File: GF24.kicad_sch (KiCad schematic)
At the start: 1 part, among them U1 STM32F031C4Tx

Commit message: updated power
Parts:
- added C1, C2: 4.7uF, symbol Device:C
- added C3: 10nF, symbol Device:C
- U1: value STM32F031C4Tx -> STM32F031C4T6
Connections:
- net +3V3: now reaches U1.1 (VBAT)
- net +3V3: now also U1.24 (VDD), U1.48 (VDD), U1.9 (VDDA), C1.1, C2.1, C3.1
- net GND: now reaches U1.23 (VSS), U1.47 (VSS)
- net GND: now also U1.8 (VSSA), C1.2, C2.2, C3.2

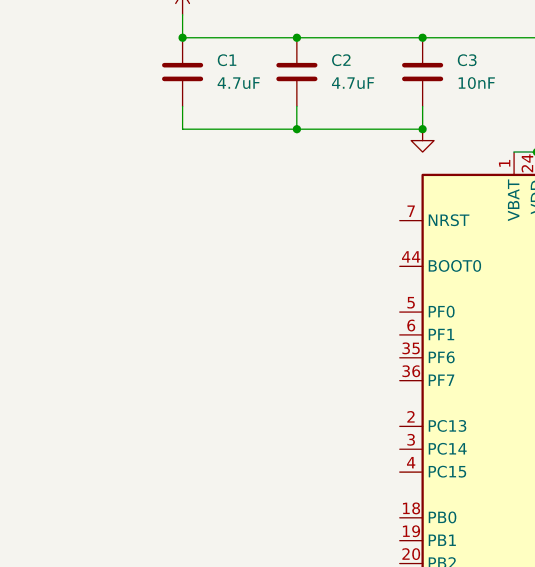
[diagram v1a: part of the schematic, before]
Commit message: changed NRST
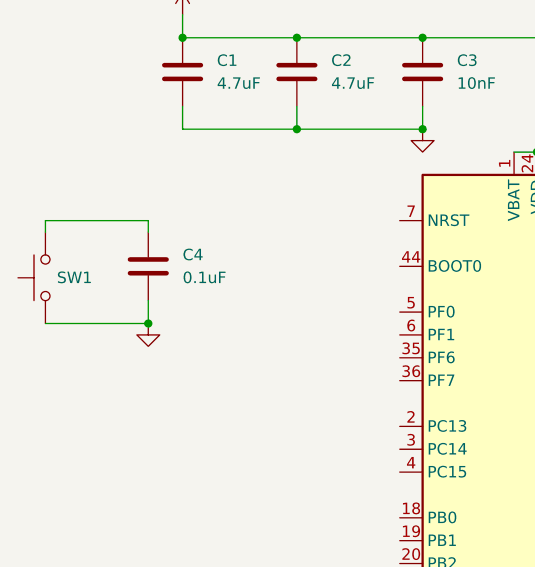
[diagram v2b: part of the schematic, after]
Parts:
- added C4: 0.1uF, symbol Device:C
- added SW1: RST, symbol Switch:SW_Push
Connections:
- net GND: now also C4.2, SW1.1
- new net: C4.1, SW1.2

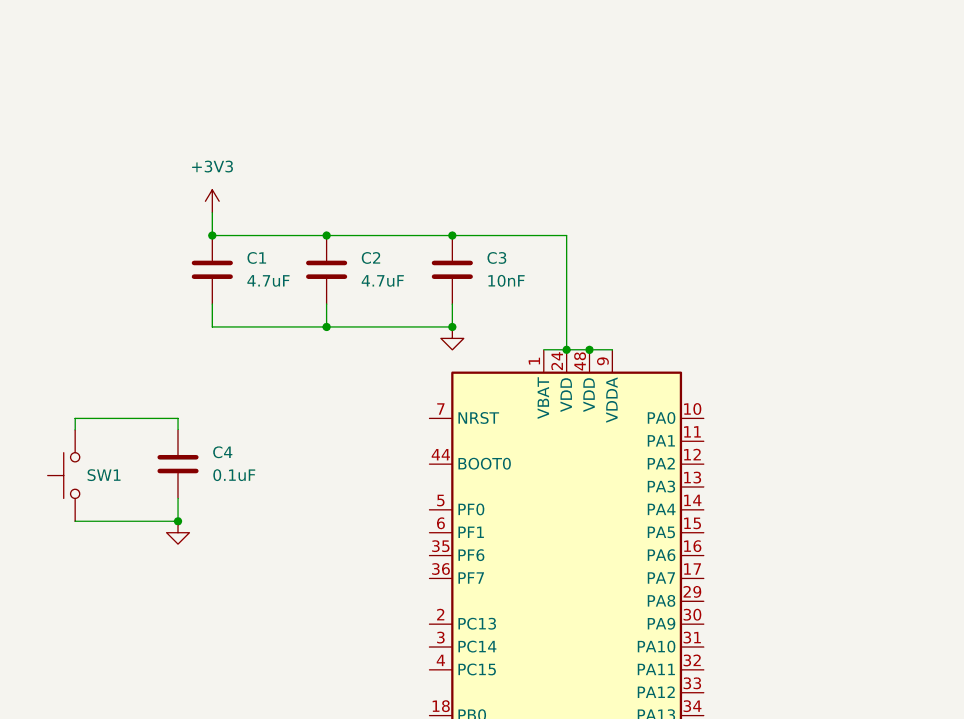
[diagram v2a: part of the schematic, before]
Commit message: sorted BOOT0 for now, added HSE
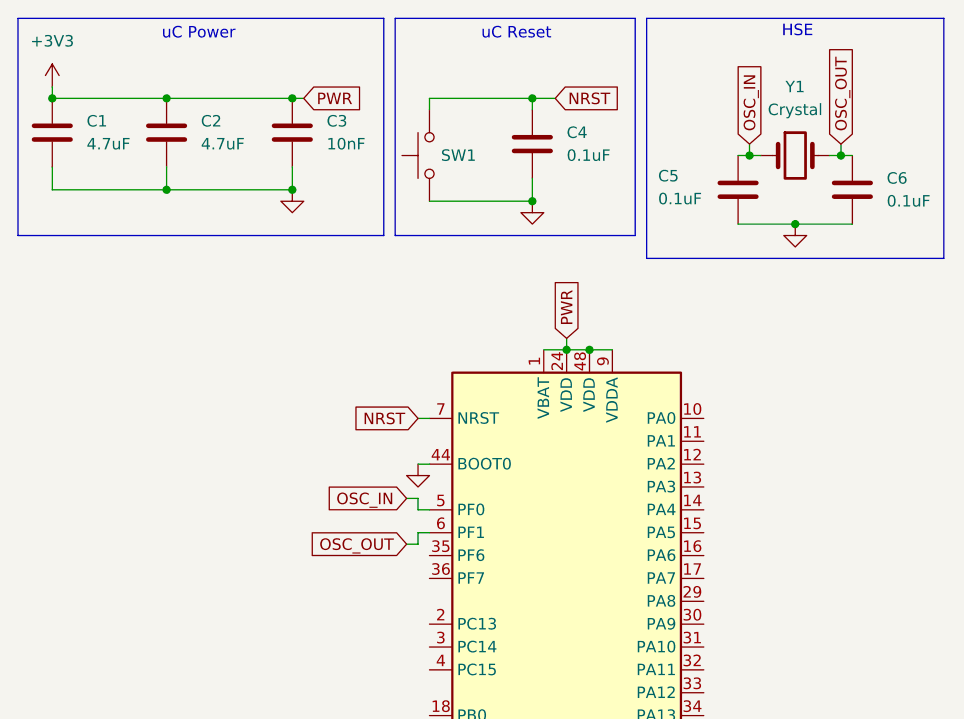
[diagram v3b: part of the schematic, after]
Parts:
- added C5, C6: 0.1uF, symbol Device:C
- added Y1: Crystal, symbol Device:Crystal
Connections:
- net GND: now also U1.44 (BOOT0), C5.2, C6.2
- net NRST: now reaches C4.1, SW1.2
- net NRST: now also U1.7 (NRST)
- net OSC_IN: now reaches U1.5 (PF0)
- net OSC_IN: now also C5.1, Y1.1
- net OSC_OUT: now reaches U1.6 (PF1)
- net OSC_OUT: now also C6.1, Y1.2
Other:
- note added: "HSE"
- note added: "uC Power"
- note added: "uC Reset"
- moved on the sheet: C1, C2, C3, C4, SW1

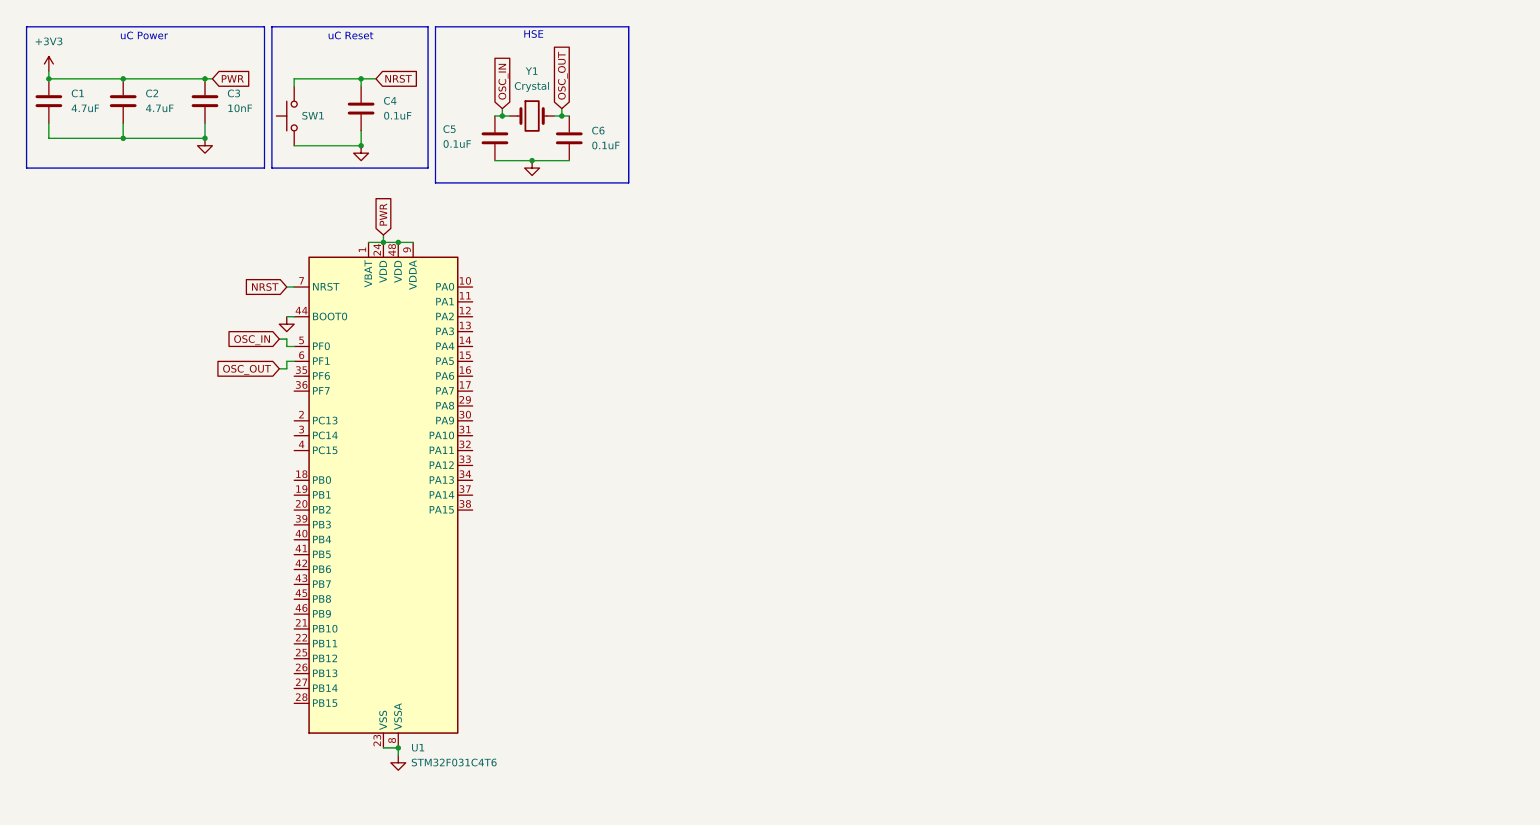
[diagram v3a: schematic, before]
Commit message: added MAX-M10S symbol/footprint
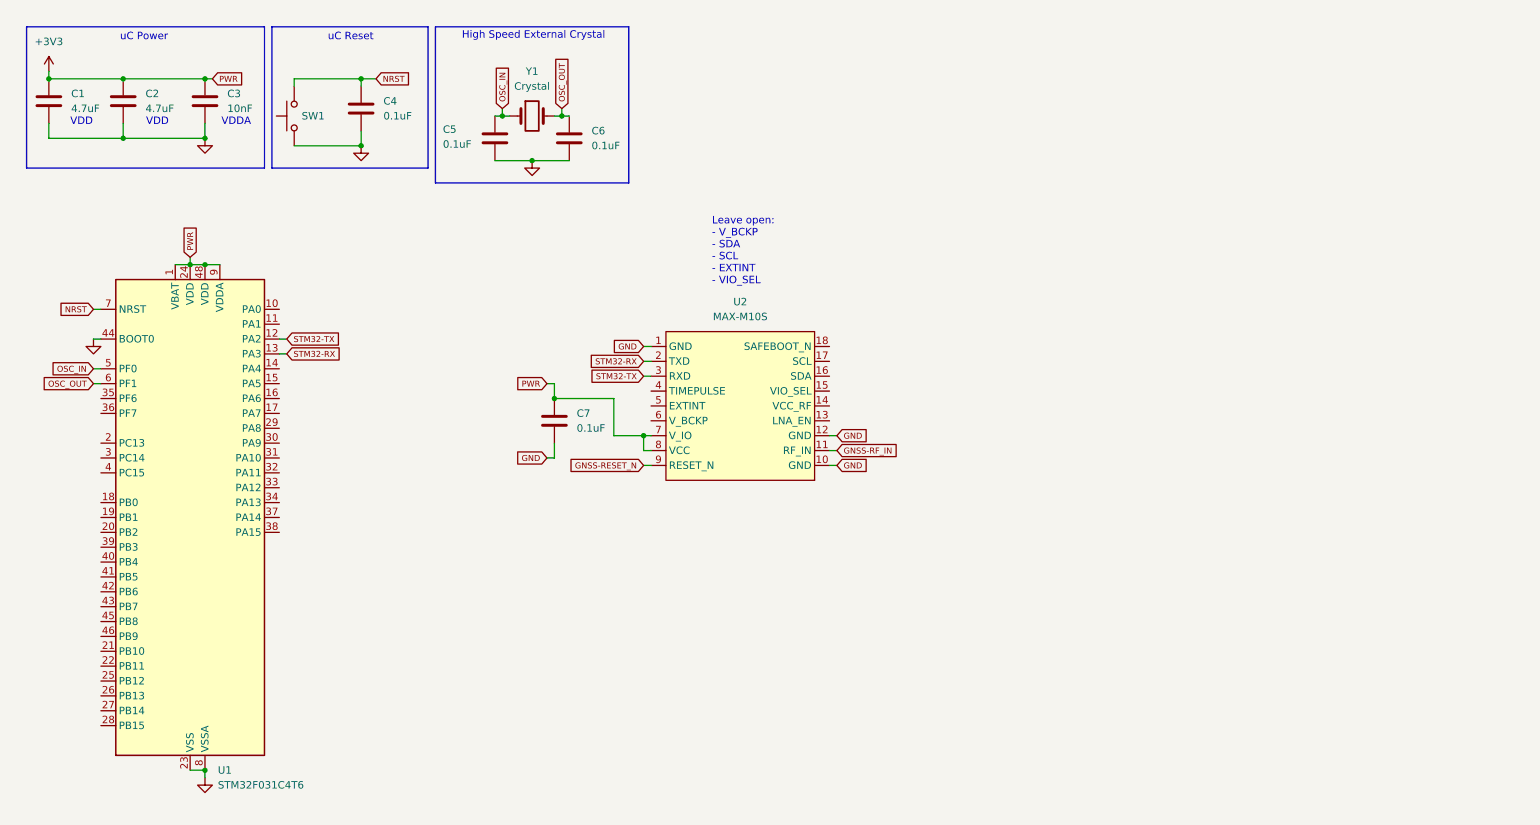
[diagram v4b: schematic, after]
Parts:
- added C7: 0.1uF, symbol Device:C
- added U2: MAX-M10S, MB-GNSS:MAX-M10S, symbol MB-GNSS:MAX-M10S
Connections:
- net +3V3: now also C7.1, U2.7 (V_IO), U2.8 (VCC)
- net GND: now also C7.2, U2.1 (GND), U2.10 (GND), U2.12 (GND)
- net STM32-TX: now reaches U1.12 (PA2)
- net STM32-TX: now also U2.3 (RXD)
- net STM32-RX: now reaches U1.13 (PA3)
- net STM32-RX: now also U2.2 (TXD)
- new net GNSS-RESET_N: U2.9 (RESET_N)
- new net GNSS-RF_IN: U2.11 (RF_IN)
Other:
- note added: "High Speed External Crystal"
- note added: "Leave open: - V_BCKP - SDA - SCL - EXTINT - VIO_SEL"
- note added: "VDD"
- note added: "VDDA"
- note removed: "HSE"
- moved on the sheet: U1

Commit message: didn't update
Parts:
- C7: value 0.1uF -> 4.7uF
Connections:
- net GNSS-RESET_N renamed GNSS-RESET-N
- net GNSS-RF_IN renamed GNSS-RF-IN
- net OSC_IN renamed OSC-IN
- net OSC_OUT renamed OSC-OUT
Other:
- note added: "Leave open: - V_BCKP - SDA - SCL - EXTINT - VIO_SEL - TIMEPULSE"
- note removed: "Leave open: - V_BCKP - SDA - SCL - EXTINT - VIO_SEL"
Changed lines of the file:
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@@
 		)
 	)
-	(text "Leave open:\n- V_BCKP\n- SDA\n- SCL\n- EXTINT\n- VIO_SEL\n"
-		(exclude_from_sim no)
-		(at 132.334 53.594 0)
+	(text "Leave open:\n- V_BCKP\n- SDA\n- SCL\n- EXTINT\n- VIO_SEL\n- TIMEPULSE"
+		(exclude_from_sim no)
+		(at 131.826 101.346 0)
 		(effects
 			(font
@@
 		)
 	)
+	(global_label "GND"
+		(shape input)
+		(at 45.72 143.51 270)
+		(fields_autoplaced yes)
+		(effects
+			(font
+				(size 1.016 1.016)
+			)
+			(justify right)
+		)
+		(property "Intersheetrefs" "${INTERSHEET_REFS}"
+			(at 45.72 148.9943 90)
+			(effects
+				(font
+					(size 1.27 1.27)
+				)
+				(justify right)
+				(hide yes)
+			)
+		)
+	)
 	(global_label "PWR"
 		(shape input)
@@
 		)
 	)
-	(global_label "GNSS-RESET_N"
+	(global_label "GNSS-RESET-N"
 		(shape input)
 		(at 120.65 90.17 180)
@@
 		)
 		(property "Intersheetrefs" "${INTERSHEET_REFS}"
-			(at 106.554 90.17 0)
+			(at 106.0702 90.17 0)
 			(effects
 				(font
@@
 		)
 	)
-	(global_label "GNSS-RF_IN"
+	(global_label "GNSS-RF-IN"
 		(shape input)
 		(at 153.67 87.63 0)
@@
 		)
 		(property "Intersheetrefs" "${INTERSHEET_REFS}"
-			(at 165.5406 87.63 0)
+			(at 166.0244 87.63 0)
 			(effects
 				(font
@@
 		)
 	)
-	(global_label "OSC_OUT"
+	(global_label "OSC-OUT"
 		(shape input)
 		(at 106.68 29.21 90)
@@
 		)
 		(property "Intersheetrefs" "${INTERSHEET_REFS}"
-			(at 106.68 20.0971 90)
-			(effects
-				(font
-					(size 1.27 1.27)
-				)
-				(justify left)
-				(hide yes)
-			)
-		)
-	)
-	(global_label "OSC_OUT"
+			(at 106.68 19.6133 90)
+			(effects
+				(font
+					(size 1.27 1.27)
+				)
+				(justify left)
+				(hide yes)
+			)
+		)
+	)
+	(global_label "OSC-OUT"
 		(shape input)
 		(at 26.67 76.2 180)
@@
 		)
 		(property "Intersheetrefs" "${INTERSHEET_REFS}"
-			(at 17.5571 76.2 0)
+			(at 17.0733 76.2 0)
 			(effects
 				(font
@@
 		)
 	)
+	(global_label "GND"
+		(shape input)
+		(at 26.67 68.58 180)
+		(fields_autoplaced yes)
+		(effects
+			(font
+				(size 1.016 1.016)
+			)
+			(justify right)
+		)
+		(property "Intersheetrefs" "${INTERSHEET_REFS}"
+			(at 21.1857 68.58 0)
+			(effects
+				(font
+					(size 1.27 1.27)
+				)
+				(justify right)
+				(hide yes)
+			)
+		)
+	)
 	(global_label "NRST"
 		(shape input)
@@
 		)
 	)
-	(global_label "OSC_IN"
+	(global_label "OSC-IN"
 		(shape input)
 		(at 96.52 29.21 90)
@@
 		)
 		(property "Intersheetrefs" "${INTERSHEET_REFS}"
-			(at 96.52 21.4518 90)
-			(effects
-				(font
-					(size 1.27 1.27)
-				)
-				(justify left)
-				(hide yes)
-			)
-		)
-	)
-	(global_label "OSC_IN"
+			(at 96.52 20.968 90)
+			(effects
+				(font
+					(size 1.27 1.27)
+				)
+				(justify left)
+				(hide yes)
+			)
+		)
+	)
+	(global_label "OSC-IN"
 		(shape input)
 		(at 26.67 73.66 180)
@@
 		)
 		(property "Intersheetrefs" "${INTERSHEET_REFS}"
-			(at 18.9118 73.66 0)
+			(at 18.428 73.66 0)
 			(effects
 				(font
@@
 			)
 		)
-		(property "Value" "0.1uF"
+		(property "Value" "4.7uF"
 			(at 109.22 83.8199 0)
 			(effects
@@
 	)
 	(symbol
-		(lib_id "power:GND")
-		(at 26.67 68.58 0)
-		(unit 1)
-		(exclude_from_sim no)
-		(in_bom yes)
-		(on_board yes)
-		(dnp no)
-		(fields_autoplaced yes)
-		(property "Reference" "#PWR05"
-			(at 26.67 74.93 0)
-			(effects
-				(font
-					(size 1.27 1.27)
-				)
-				(hide yes)
-			)
-		)
-		(property "Value" "GND"
-			(at 26.67 73.66 0)
-			(show_name yes)
-			(effects
-				(font
-					(size 1.27 1.27)
-				)
-				(hide yes)
-			)
-		)
-		(property "Footprint" ""
-			(at 26.67 68.58 0)
-			(effects
-				(font
-					(size 1.27 1.27)
-				)
-				(hide yes)
-			)
-		)
-		(property "Datasheet" ""
-			(at 26.67 68.58 0)
-			(effects
-				(font
-					(size 1.27 1.27)
-				)
-				(hide yes)
-			)
-		)
-		(property "Description" "Power symbol creates a global label with name \"GND\" , ground"
-			(at 26.67 68.58 0)
-			(effects
-				(font
-					(size 1.27 1.27)
-				)
-				(hide yes)
-			)
-		)
-		(pin "1"
-		)
-		(instances
-			(project "GF24"
-				(path "/d7f5d038-1fc1-4384-87c8-ac3b01beb09a"
-					(reference "#PWR05")
-					(unit 1)
-				)
-			)
-		)
-	)
-	(symbol
 		(lib_id "power:+3V3")
 		(at 19.05 22.86 0)
@@
 					(unit 1)
 				)
-			)
-		)
-	)
-	(symbol
-		(lib_id "power:GND")
-		(at 45.72 143.51 0)
-		(unit 1)
-		(exclude_from_sim no)
-		(in_bom yes)
-		(on_board yes)
-		(dnp no)
-		(fields_autoplaced yes)
-		(property "Reference" "#PWR03"
-			(at 45.72 149.86 0)
-			(effects
-				(font
-					(size 1.27 1.27)
-				)
-				(hide yes)
-			)
-		)
-		(property "Value" "GND"
-			(at 45.72 148.59 0)
-			(show_name yes)
-			(effects
-				(font
-					(size 1.27 1.27)
-				)
-				(hide yes)
-			)
-		)
-		(property "Footprint" ""
-			(at 45.72 143.51 0)
-			(effects
-				(font
-					(size 1.27 1.27)
-				)
-				(hide yes)
-			)
-		)
-		(property "Datasheet" ""
-			(at 45.72 143.51 0)
-			(effects
-				(font
-					(size 1.27 1.27)
-				)
-				(hide yes)
-			)
-		)
-		(property "Description" "Power symbol creates a global label with name \"GND\" , ground"
-			(at 45.72 143.51 0)
-			(effects
-				(font
-					(size 1.27 1.27)
-				)
-				(hide yes)
-			)
-		)
-		(pin "1"
-		)
-		(instances
-			(project "GF24"
-				(path "/d7f5d038-1fc1-4384-87c8-ac3b01beb09a"
-					(reference "#PWR03")
-					(unit 1)
-				)

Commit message: added cap footprints
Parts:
- C1, C2, C3: footprint (none) -> Capacitor_SMD:C_1210_3225Metric_Pad1.33x2.70mm_HandSolder
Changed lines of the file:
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@@
 			)
 		)
-		(property "Footprint" ""
+		(property "Footprint" "Capacitor_SMD:C_1210_3225Metric_Pad1.33x2.70mm_HandSolder"
 			(at 32.7152 31.75 0)
 			(effects
@@
 			)
 		)
-		(property "Description" "Unpolarized capacitor"
+		(property "Description" "Unpolarized capacitor, C1210C475K5RACTU"
 			(at 31.75 27.94 0)
 			(effects
@@
 			)
 		)
-		(property "Footprint" ""
+		(property "Footprint" "Capacitor_SMD:C_1210_3225Metric_Pad1.33x2.70mm_HandSolder"
 			(at 20.0152 31.75 0)
 			(effects
@@
 			)
 		)
-		(property "Description" "Unpolarized capacitor"
+		(property "Description" "Unpolarized capacitor, C1210C475K5RACTU"
 			(at 19.05 27.94 0)
 			(effects
@@
 			)
 		)
-		(property "Footprint" ""
+		(property "Footprint" "Capacitor_SMD:C_1210_3225Metric_Pad1.33x2.70mm_HandSolder"
 			(at 46.6852 31.75 0)
 			(effects
@@
 			)
 		)
-		(property "Description" "Unpolarized capacitor"
+		(property "Description" "Unpolarized capacitor, C1210C103K5RACTU"
 			(at 45.72 27.94 0)
 			(effects
